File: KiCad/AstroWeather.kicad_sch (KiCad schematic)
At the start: 16 parts, among them J101 I2C, J102 Conn_01x10, J103 SWD, J104 Conn_01x10, J105 AUX_POWER, J106 USB, U101 INA180A2

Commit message: Display submit synchronization
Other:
- note added: "Bugs: Missing voltage divider on input voltage sense SENSE inputs connected to non-ADC pins Vref shorted to GND - fix by connecting to Vdd"
- note removed: "Bugs: Missing voltage divider on input voltage sense SENSE inputs connected to non-ADC pins Vref shorted to GND"
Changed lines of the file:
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@@
 		)
 	)
-	(text "Bugs:\nMissing voltage divider on input voltage sense\nSENSE inputs connected to non-ADC pins\nVref shorted to GND"
+	(text "Bugs:\nMissing voltage divider on input voltage sense\nSENSE inputs connected to non-ADC pins\nVref shorted to GND - fix by connecting to Vdd"
 		(exclude_from_sim no)
 		(at 18.796 24.13 0)

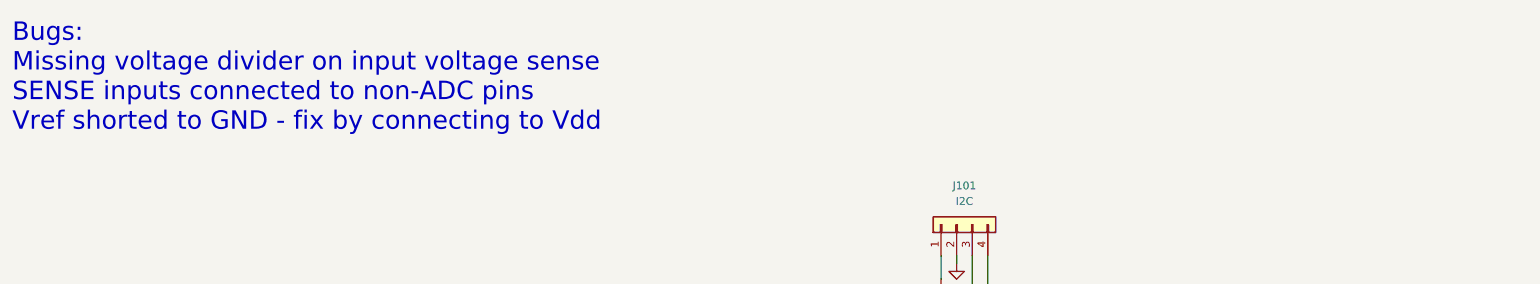
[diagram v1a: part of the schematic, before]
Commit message: RC values fixed
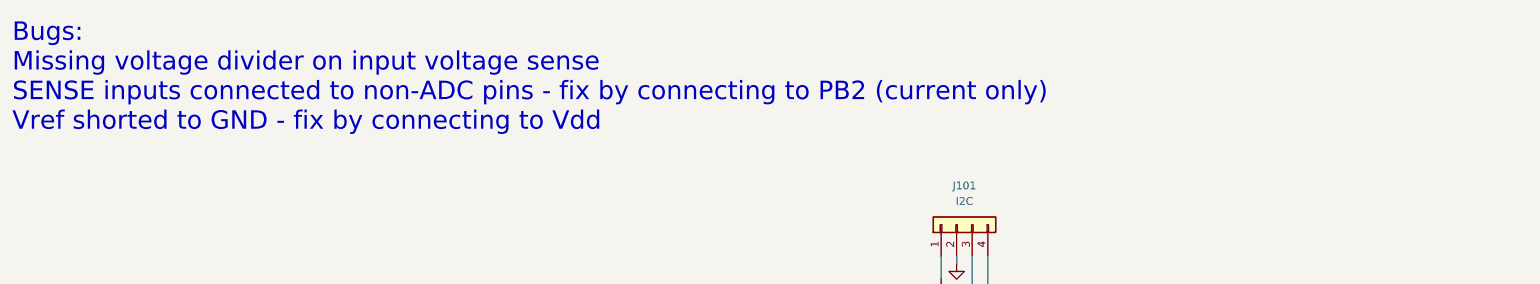
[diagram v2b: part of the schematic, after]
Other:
- note added: "Bugs: Missing voltage divider on input voltage sense SENSE inputs connected to non-ADC pins - fix by connecting to PB2 (current only) Vref shorted to GND - fix by connecting to Vdd"
- note removed: "Bugs: Missing voltage divider on input voltage sense SENSE inputs connected to non-ADC pins Vref shorted to GND - fix by connecting to Vdd"
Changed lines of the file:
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@@
 		)
 	)
-	(text "Bugs:\nMissing voltage divider on input voltage sense\nSENSE inputs connected to non-ADC pins\nVref shorted to GND - fix by connecting to Vdd"
+	(text "Bugs:\nMissing voltage divider on input voltage sense\nSENSE inputs connected to non-ADC pins - fix by connecting to PB2 (current only)\nVref shorted to GND - fix by connecting to Vdd"
 		(exclude_from_sim no)
 		(at 18.796 24.13 0)

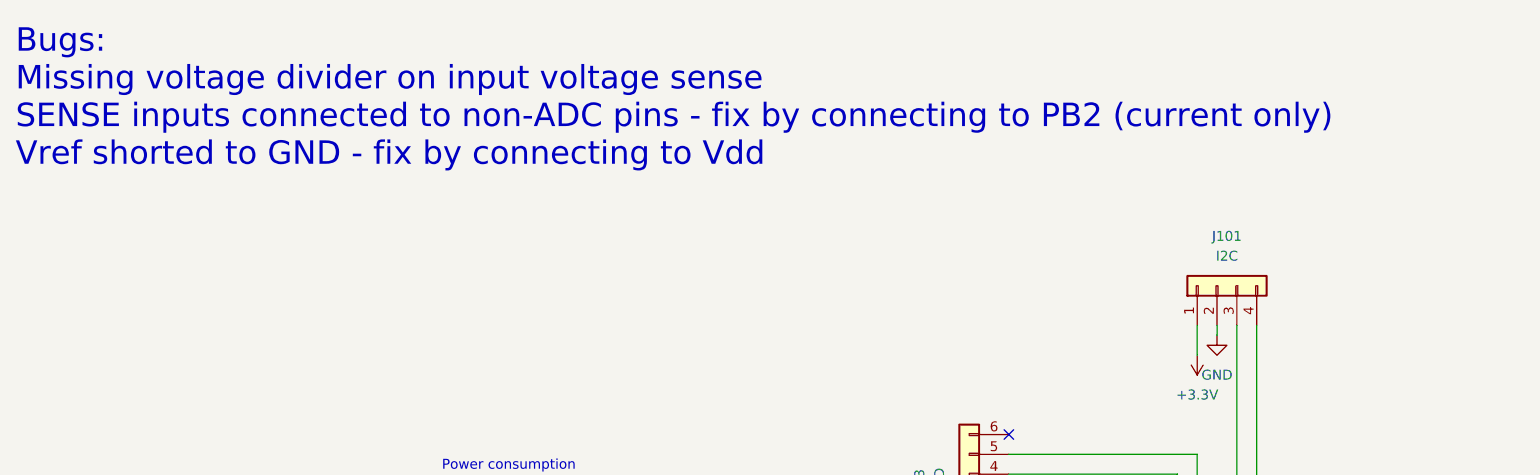
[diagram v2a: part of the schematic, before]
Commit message: Console commands extracted to separate files
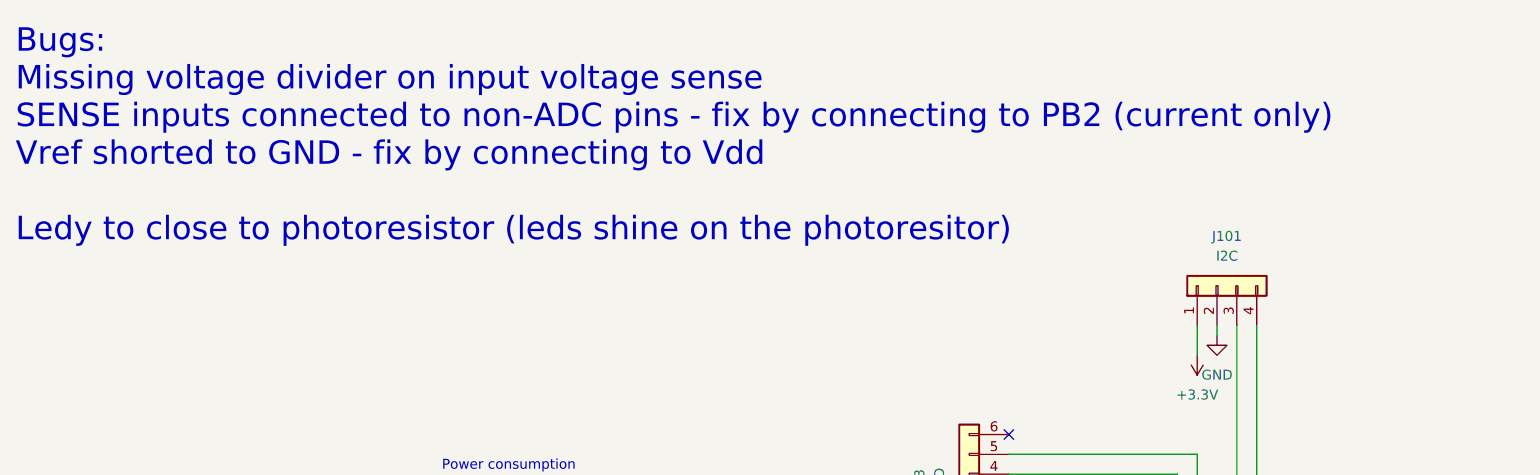
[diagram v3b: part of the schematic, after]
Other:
- note added: "Bugs: Missing voltage divider on input voltage sense SENSE inputs connected to non-ADC pins - fix by connecting to PB2 (current only) Vref shorted to GND - fix by connecting to Vdd Ledy to close to photoresistor (leds shine on the photoresitor)"
- note removed: "Bugs: Missing voltage divider on input voltage sense SENSE inputs connected to non-ADC pins - fix by connecting to PB2 (current only) Vref shorted to GND - fix by connecting to Vdd"
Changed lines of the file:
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@@
 		)
 	)
-	(text "Bugs:\nMissing voltage divider on input voltage sense\nSENSE inputs connected to non-ADC pins - fix by connecting to PB2 (current only)\nVref shorted to GND - fix by connecting to Vdd"
+	(text "Bugs:\nMissing voltage divider on input voltage sense\nSENSE inputs connected to non-ADC pins - fix by connecting to PB2 (current only)\nVref shorted to GND - fix by connecting to Vdd\n\nLedy to close to photoresistor (leds shine on the photoresitor)"
 		(exclude_from_sim no)
 		(at 18.796 24.13 0)
